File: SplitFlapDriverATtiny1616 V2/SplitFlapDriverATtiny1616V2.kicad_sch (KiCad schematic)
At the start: 17 parts, among them J1 UPDI Programming, J2 BUS POGO, J3 Stepper Connector, J4 Hall Effect, J5 Conn_01x06_Pin, U1 ATtiny1616-MNR, U2 ULN2003ADR, U3 SN65HVD72DR, U5 SPX3819M5-L-3-3

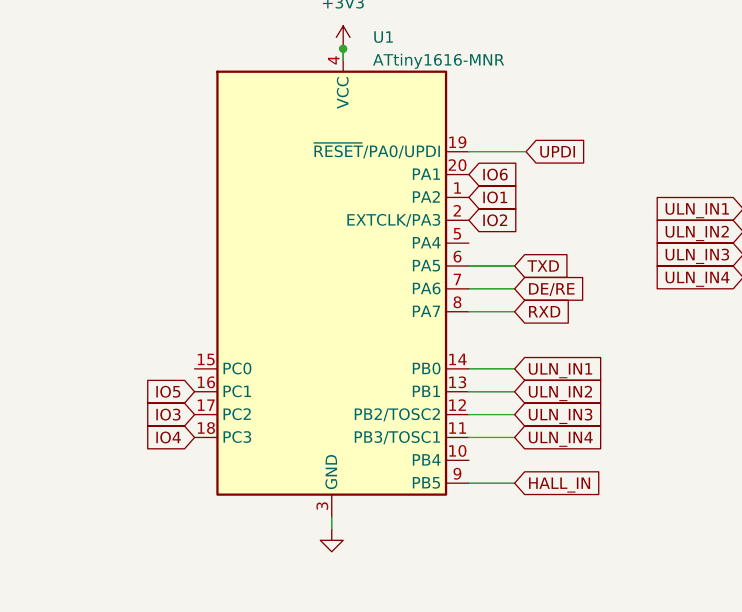
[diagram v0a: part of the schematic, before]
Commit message: Added SplitFlapBusBoard
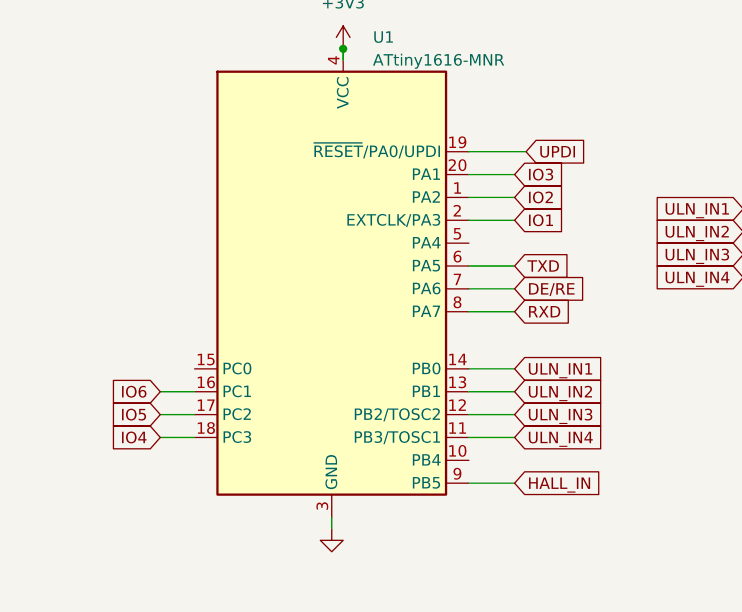
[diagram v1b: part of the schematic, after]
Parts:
- J5: footprint Connector_PinSocket_2.54mm:PinSocket_1x06_P2.54mm_Vertical -> Connector_PinHeader_2.54mm:PinHeader_1x06_P2.54mm_Vertical
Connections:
- net IO1: now also U1.2 (EXTCLK/PA3); no longer U1.1 (PA2)
- net IO2: now also U1.1 (PA2); no longer U1.2 (EXTCLK/PA3)
- net IO3: now also U1.20 (PA1); no longer U1.17 (PC2)
- net IO5: now also U1.17 (PC2); no longer U1.16 (PC1)
- net IO6: now also U1.16 (PC1); no longer U1.20 (PA1)

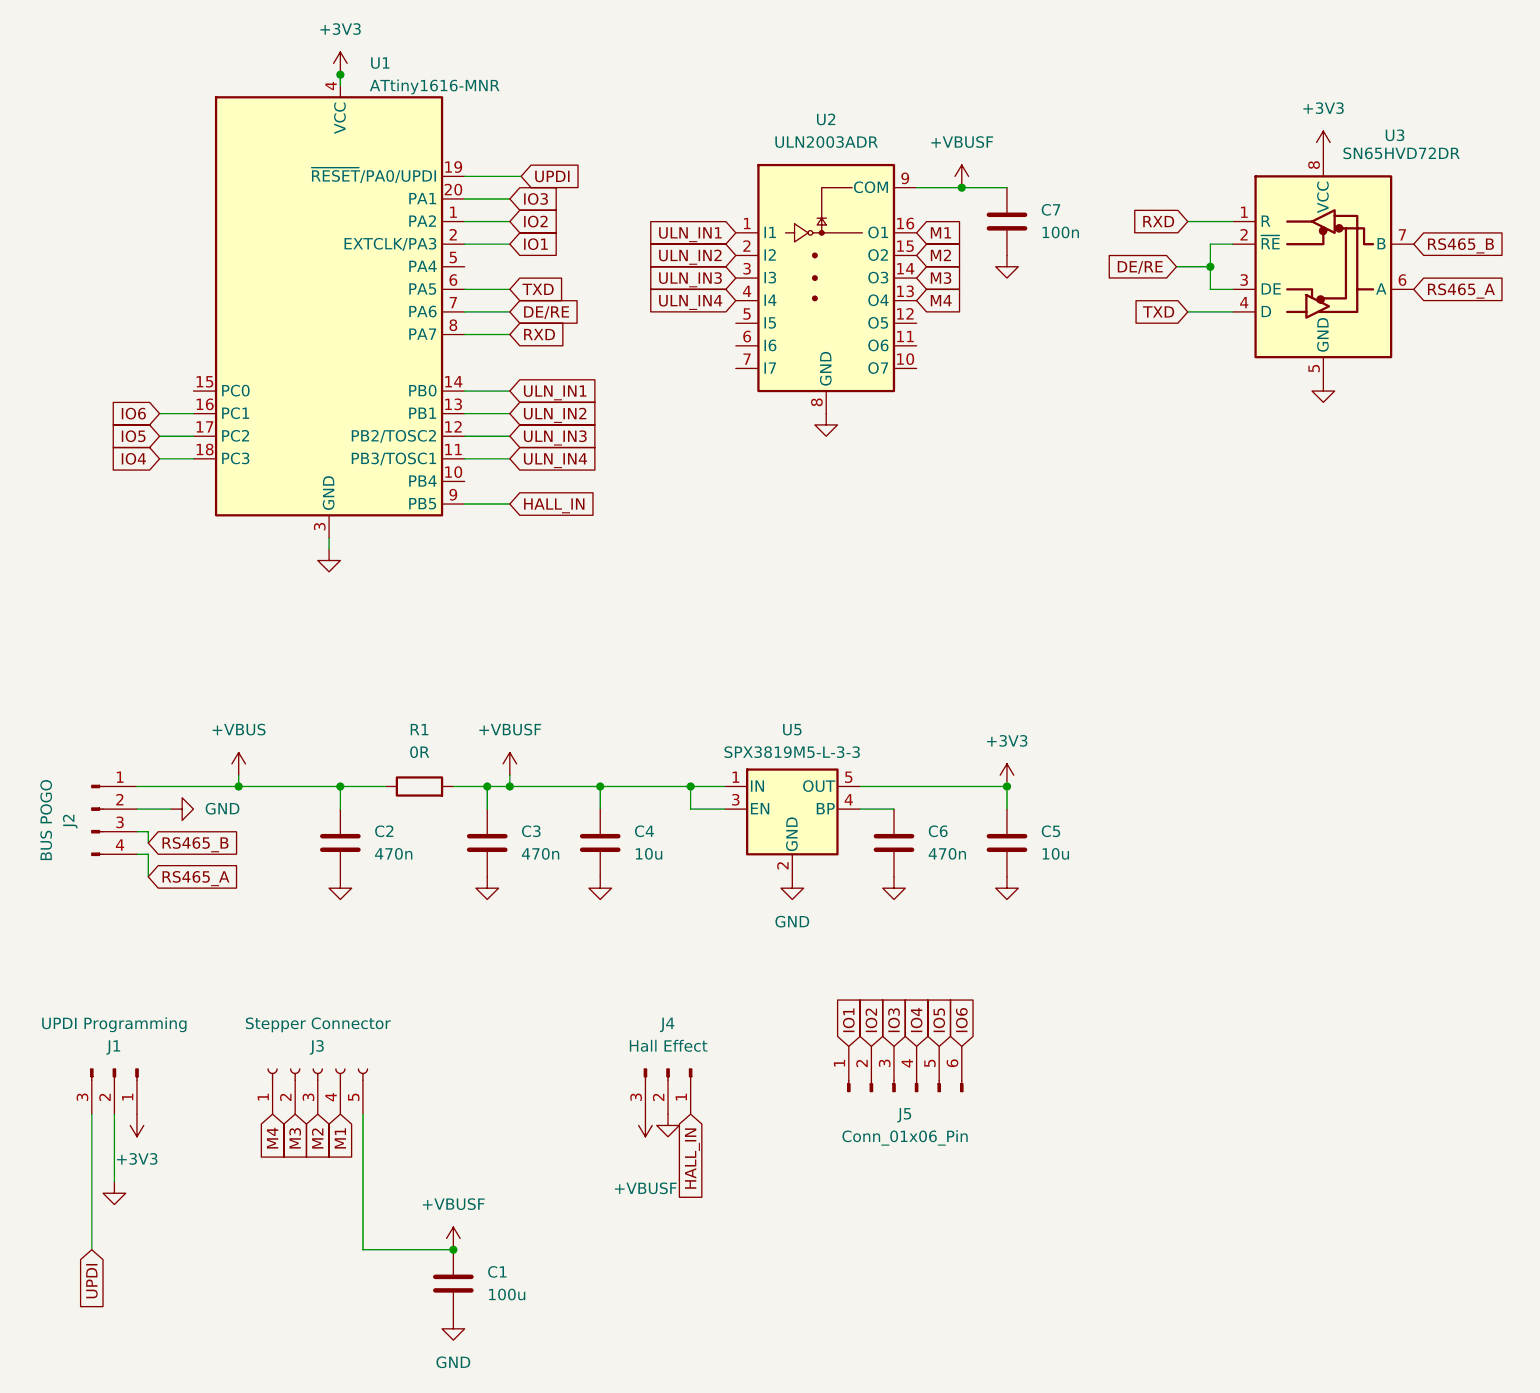
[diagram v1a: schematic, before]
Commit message: Version 2 of Hub and Module Board
Finished and ordered bus board and V2 or Module board (50x)
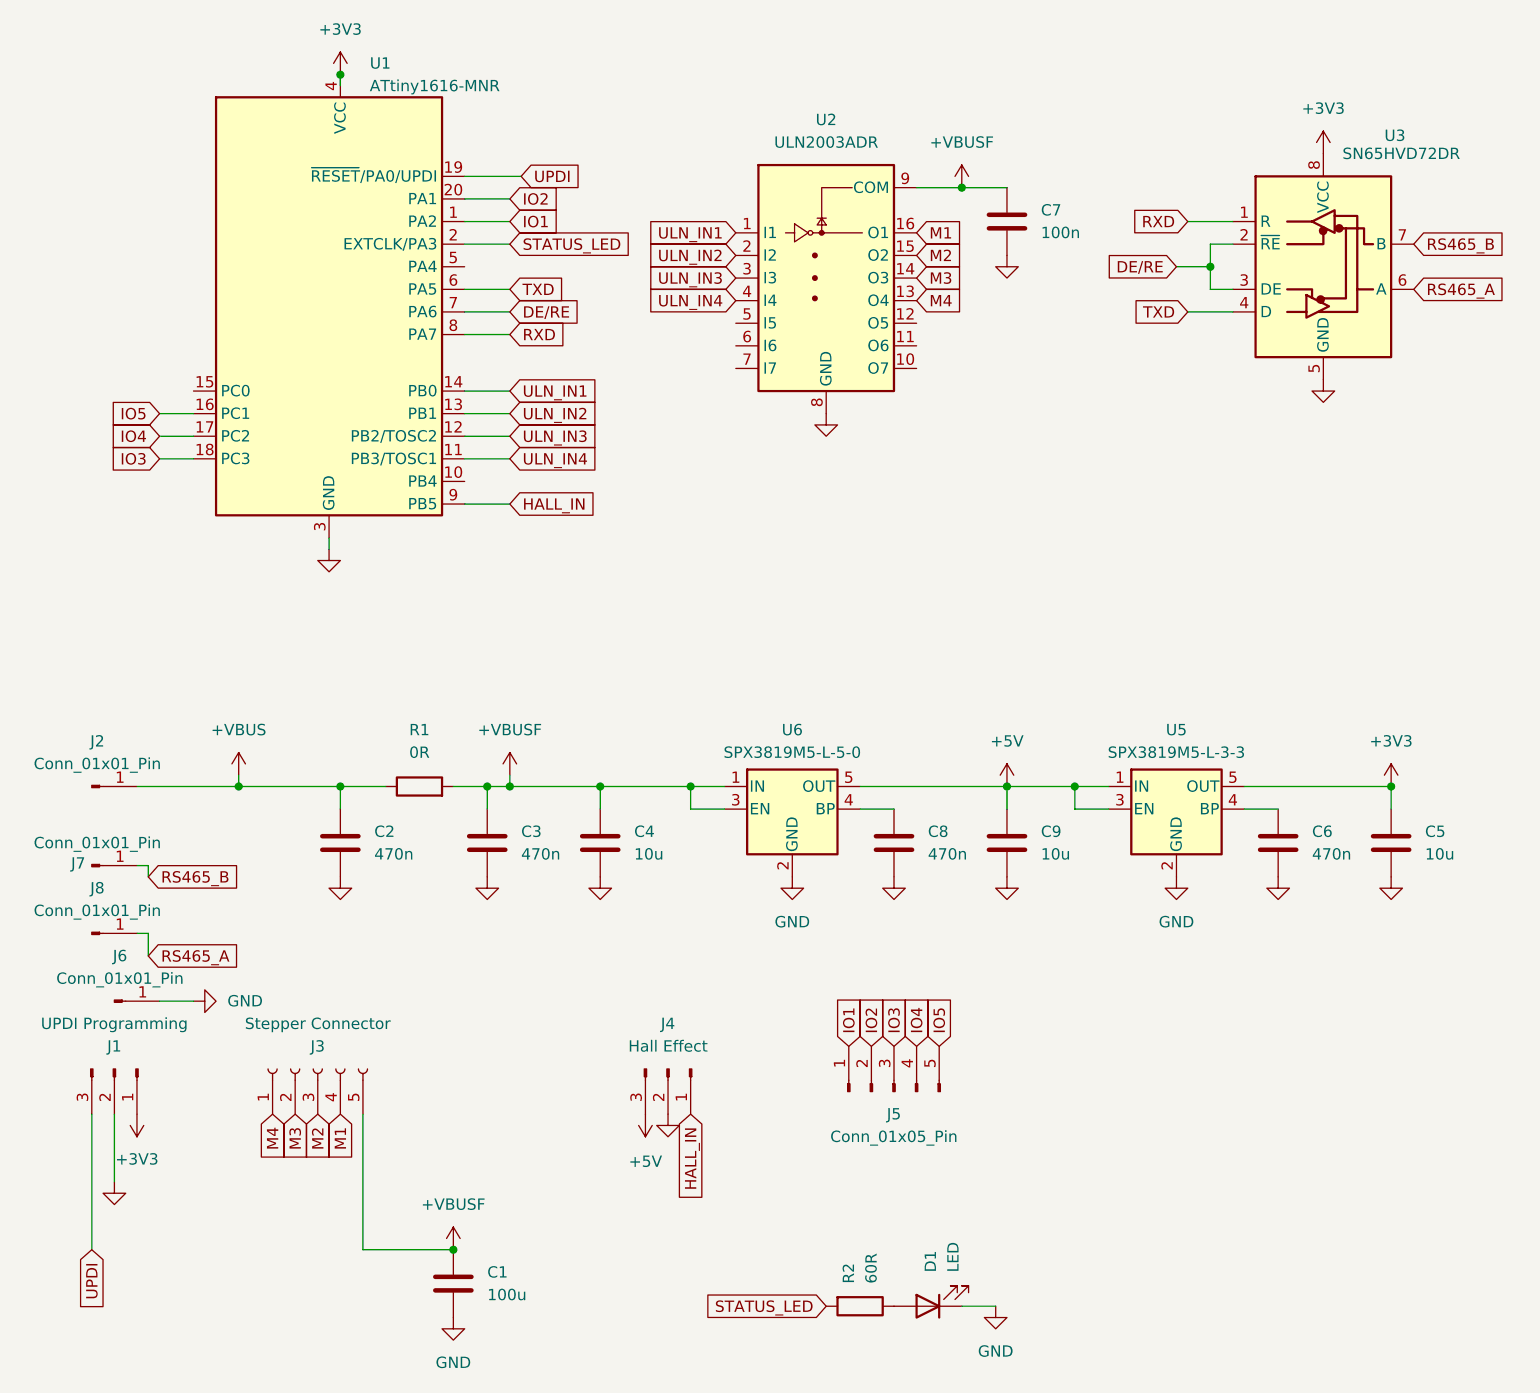
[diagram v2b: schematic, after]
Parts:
- removed J2: BUS POGO, Connector_PinHeader_2.54mm:PinHeader_1x04_P2.54mm_Vertical, symbol Connector:Conn_01x04_Pin
- added C8: 470n, Capacitor_SMD:C_0603_1608Metric, symbol Device:C
- added C9: 10u, Capacitor_SMD:C_0603_1608Metric, symbol Device:C
- added D1: LED, LED_SMD:LED_0201_0603Metric, symbol Device:LED
- added J2, J6, J7, J8: Conn_01x01_Pin, Connector_PinHeader_2.54mm:PinHeader_1x01_P2.54mm_Vertical, symbol Connector:Conn_01x01_Pin
- added R2: 60R, Resistor_SMD:R_0201_0603Metric, symbol Device:R
- added U6: SPX3819M5-L-5-0, Package_TO_SOT_SMD:SOT-23-5, symbol Regulator_Linear:SPX3819M5-L-5-0
- J5: value Conn_01x06_Pin -> Conn_01x05_Pin; footprint Connector_PinHeader_2.54mm:PinHeader_1x06_P2.54mm_Vertical -> Connector_PinHeader_2.54mm:PinHeader_1x05_P2.54mm_Vertical; symbol Connector:Conn_01x06_Pin -> Connector:Conn_01x05_Pin
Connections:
- net +VBUS: now also J2.1 (Pin_1)
- net +VBUSF: now also U6.1 (IN), U6.3 (EN); no longer J4.3 (Pin_3), U5.1 (IN), U5.3 (EN)
- net GND: now also C8.2, C9.2, D1.1 (K), J6.1 (Pin_1), U6.2 (GND)
- net IO1: now also U1.1 (PA2); no longer U1.2 (EXTCLK/PA3)
- net IO2: now also U1.20 (PA1); no longer U1.1 (PA2)
- net IO3: now also U1.18 (PC3); no longer U1.20 (PA1)
- net IO4: now also U1.17 (PC2); no longer U1.18 (PC3)
- net IO5: now also U1.16 (PC1); no longer U1.17 (PC2)
- net RS465_A: now also J8.1 (Pin_1)
- net RS465_B: now also J7.1 (Pin_1)
- removed net IO6: J5.6 (Pin_6), U1.16 (PC1)
- new net: D1.2 (A), R2.1
- new net: C8.1, U6.4 (BP)
- new net +5V: C9.1, J4.3 (Pin_3), U5.1 (IN), U5.3 (EN), U6.5 (OUT)
- new net STATUS_LED: R2.2, U1.2 (EXTCLK/PA3)
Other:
- moved on the sheet: C5, C6, U5
